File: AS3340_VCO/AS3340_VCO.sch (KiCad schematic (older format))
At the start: 14 parts, among them J1 CV_In, J12 Conn_01x10, J2 Waveform_Out, U1 AS3340

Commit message: AS3340_VCO rev 2 AS3310_ADSR rev 1 AS3320_VCF rev 1 AS3360_VCA rev 1 ER_Bus_Board rev 1
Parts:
- removed J12: Conn_01x10, Connector_IDC:IDC-Header_2x05_P2.54mm_Vertical, symbol Connector_Generic:Conn_01x10
- added C7: 560pF, Capacitor_SMD:C_0805_2012Metric, symbol Device:C
- added C8, C9: 10uF, Capacitor_SMD:CP_Elec_4x3, symbol Device:CP1
- added J3: Power, Connector_IDC:IDC-Header_2x08_P2.54mm_Vertical, symbol Connector_Generic:Conn_01x16
- added JP5: Jumper, Connector_PinHeader_2.54mm:PinHeader_1x02_P2.54mm_Vertical, symbol Device:Jumper
- added JP6: Jumper_3_Open, Connector_PinHeader_2.54mm:PinHeader_1x03_P2.54mm_Vertical, symbol Jumper:Jumper_3_Open
- added R13: 5.6K, Resistor_SMD:R_0805_2012Metric, symbol Device:R_US
- added R43: 100K 0.05%, Resistor_SMD:R_0805_2012Metric, symbol Device:R_US
- added RV3: 1K, Potentiometer_THT:Potentiometer_Bourns_3296W_Vertical, symbol Device:R_POT_TRIM_US
- added TP1, TP2: TestPoint, TestPoint:TestPoint_Pad_D2.0mm, symbol Connector:TestPoint
- R1, R2, R3: value 100K -> 100K 0.05%
- R4: value 24K -> 18K
- R6: value 1.8K -> 1K
- RV1: value 10K -> 5K
- U1: footprint Package_SO:SOIC-16_3.9x9.9mm_P1.27mm -> Package_DIP:DIP-16_W7.62mm
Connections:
- net +12V: now also C8.1, J3.10 (Pin_10), J3.9 (Pin_9)
- net -12V: now also C9.2, J3.1 (Pin_1), J3.2 (Pin_2)
- net GNDREF: now also C7.1, C8.2, C9.1, J3.3 (Pin_3), J3.4 (Pin_4), J3.5 (Pin_5), J3.6 (Pin_6), J3.7 (Pin_7), J3.8 (Pin_8), JP5.2, JP6.1 (A), RV3.2, RV3.3; no longer R6.1
- net Input Conditioning/CV_RAW: now also R43.1
- net Vee: now also R13.1; no longer RV1.2, RV1.3
- net at R5.2, U1.2 (SCALE2): now also TP1.1
- net at R6.2, U1.14 (VS): now also C7.2, JP5.1
- new net: R13.2, RV1.2, RV1.3, TP2.1
- new net: R6.1, RV3.1
- new net: JP6.2 (C), R43.2
- new net +5V: J3.11 (Pin_11), J3.12 (Pin_12)
- new net ER_CV: J3.13 (Pin_13), J3.14 (Pin_14), JP6.3 (B)
- new net ER_GATE: J3.15 (Pin_15), J3.16 (Pin_16)
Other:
- moved on the sheet: R5

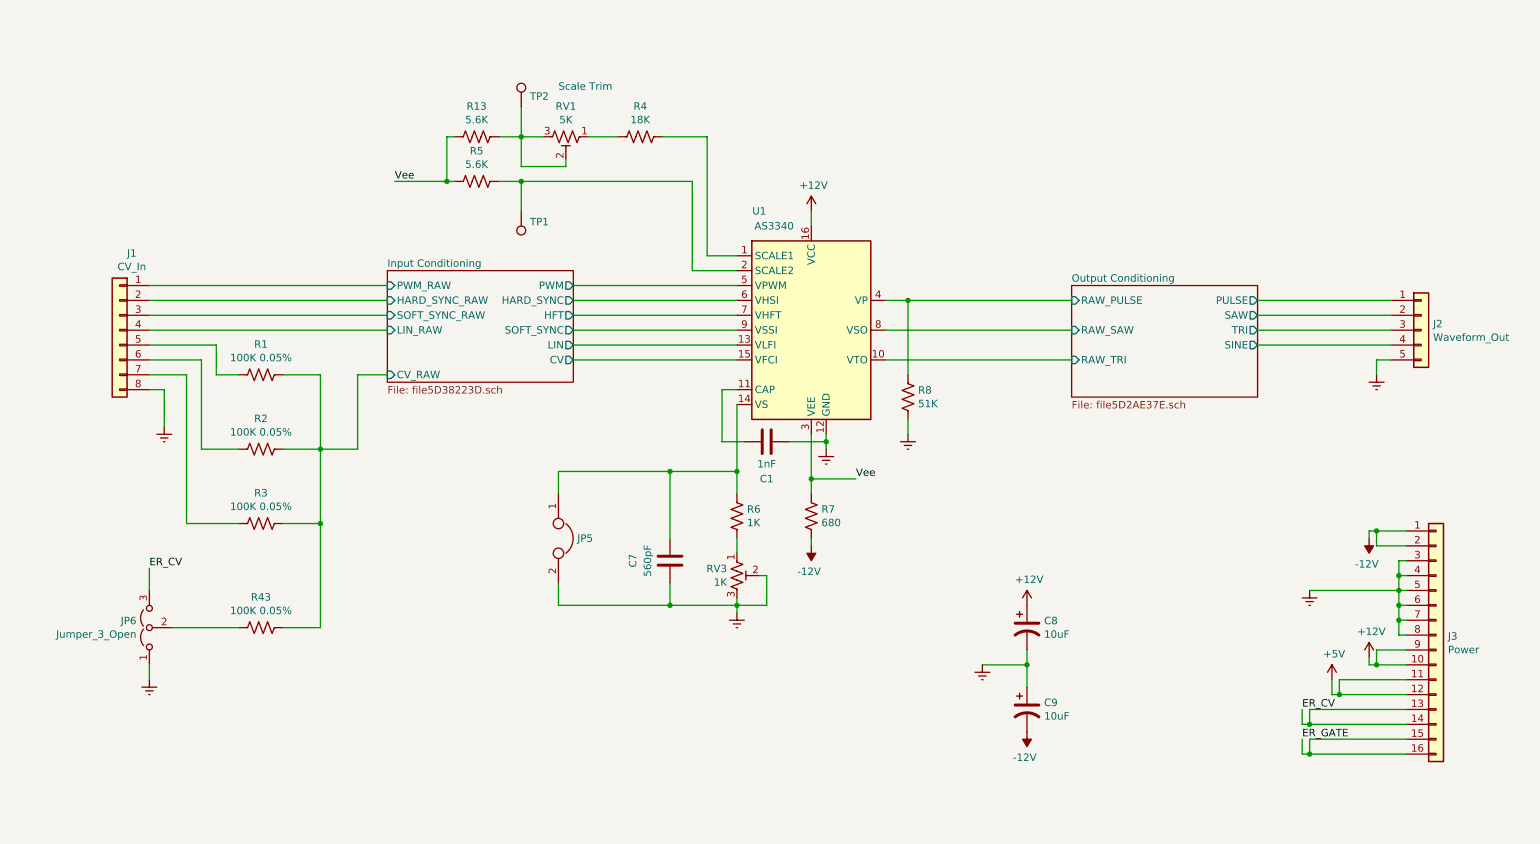
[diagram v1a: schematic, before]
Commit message: Re-do VCO board to support new front panel board
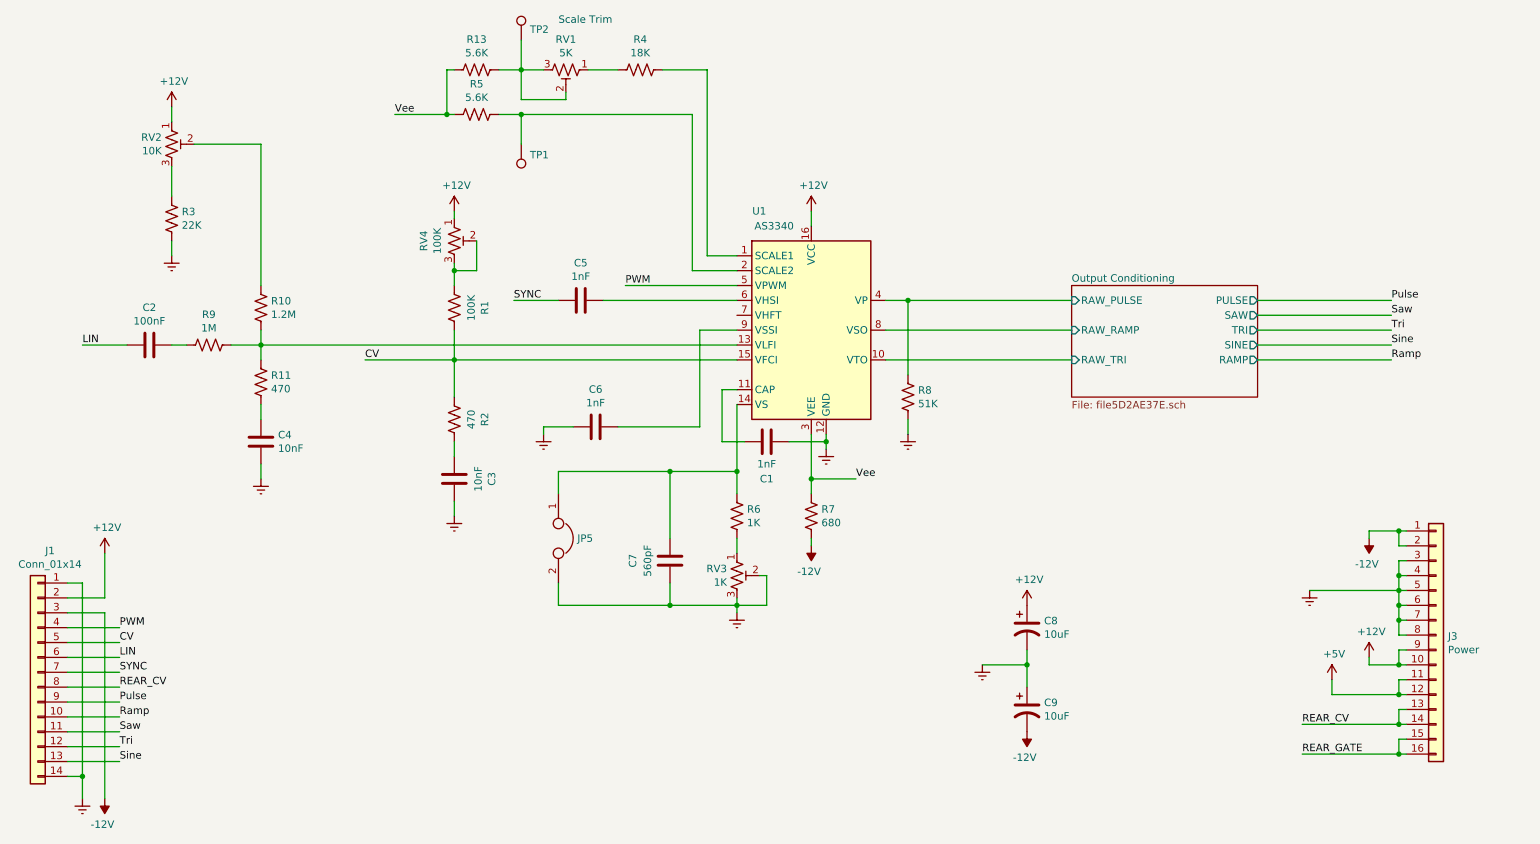
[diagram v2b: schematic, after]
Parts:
- removed J1: CV_In, Connector_PinSocket_2.54mm:PinSocket_1x08_P2.54mm_Vertical, symbol Connector_Generic:Conn_01x08
- removed J2: Waveform_Out, Connector_PinSocket_2.54mm:PinSocket_1x05_P2.54mm_Vertical, symbol Connector_Generic:Conn_01x05
- removed JP6: Jumper_3_Open, Connector_PinHeader_2.54mm:PinHeader_1x03_P2.54mm_Vertical, symbol Jumper:Jumper_3_Open
- removed R43: 100K 0.05%, Resistor_SMD:R_0805_2012Metric, symbol Device:R_US
- added C2: 100nF, Capacitor_SMD:C_0805_2012Metric, symbol Device:C
- added C3, C4: 10nF, Capacitor_SMD:C_0805_2012Metric, symbol Device:C
- added C5, C6: 1nF, Capacitor_SMD:C_0805_2012Metric, symbol Device:C
- added J1: Conn_01x14, Connector_PinHeader_2.54mm:PinHeader_1x14_P2.54mm_Vertical, symbol Connector_Generic:Conn_01x14
- added R10: 1.2M, Resistor_SMD:R_0805_2012Metric, symbol Device:R_US
- added R11: 470, Resistor_SMD:R_0805_2012Metric, symbol Device:R_US
- added R9: 1M, Resistor_SMD:R_0805_2012Metric, symbol Device:R_US
- added RV2: 10K, Potentiometer_THT:Potentiometer_Bourns_3296W_Vertical, symbol Device:R_POT_TRIM_US
- added RV4: 100K, Potentiometer_THT:Potentiometer_Bourns_3296W_Vertical, symbol Device:R_POT_TRIM_US
- R1: value 100K 0.05% -> 100K
- R2: value 100K 0.05% -> 470
- R3: value 100K 0.05% -> 22K
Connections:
- net Input Conditioning/CV is gone; now on net CV: U1.15 (VFCI)
- net +12V: now also J1.2 (Pin_2), RV2.1, RV4.1
- net -12V: now also J1.3 (Pin_3)
- net GNDREF: now also R3.1, C3.1, C4.1, C6.2, J1.1 (Pin_1), J1.14 (Pin_14)
- net at R1.2: now also RV4.2, RV4.3
- net CV: now reaches R2.2
- net CV: now also R1.1, J1.5 (Pin_5)
- net at R3.2: now also RV2.3
- net ER_CV renamed REAR_CV
- net REAR_CV: now also J1.8 (Pin_8)
- net ER_GATE renamed REAR_GATE
- removed net Input Conditioning/CV_RAW: R1.1, R2.1, R3.1
- net Input Conditioning/HARD_SYNC: no longer names the net of U1.6 (VHSI)
- net Input Conditioning/HARD_SYNC: now also C5.1
- net Input Conditioning/HFT: no longer names the net of U1.7 (VHFT)
- net Input Conditioning/LIN: no longer names the net of U1.13 (VLFI)
- net Input Conditioning/LIN: now also R10.1, R11.2, R9.1
- net Input Conditioning/PWM renamed PWM
- net PWM: now also J1.4 (Pin_4)
- net Input Conditioning/SOFT_SYNC: no longer names the net of U1.9 (VSSI)
- net Input Conditioning/SOFT_SYNC: now also C6.1
- net Output Conditioning/RAW_SAW renamed Output Conditioning/RAW_RAMP
- new net: C2.1, R9.2
- new net: R10.2, RV2.2
- new net: C4.2, R11.1
- new net: C3.2, R2.1
- new net LIN: C2.2, J1.6 (Pin_6)
- new net Pulse: J1.9 (Pin_9)
- new net Ramp: J1.10 (Pin_10)
- new net SYNC: C5.2, J1.7 (Pin_7)
- new net Saw: J1.11 (Pin_11)
- new net Sine: J1.13 (Pin_13)
- new net Tri: J1.12 (Pin_12)
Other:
- moved on the sheet: R13, R4, R5, RV1, TP1, TP2
